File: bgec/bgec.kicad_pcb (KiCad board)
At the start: 2 copper layers, 10 parts

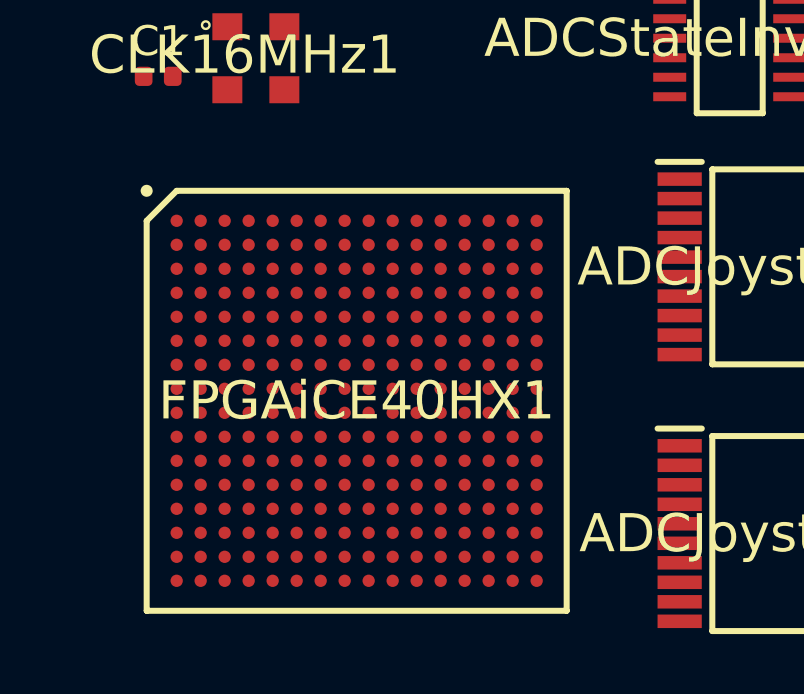
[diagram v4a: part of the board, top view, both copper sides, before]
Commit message: Switch to official footprint for the FPGA
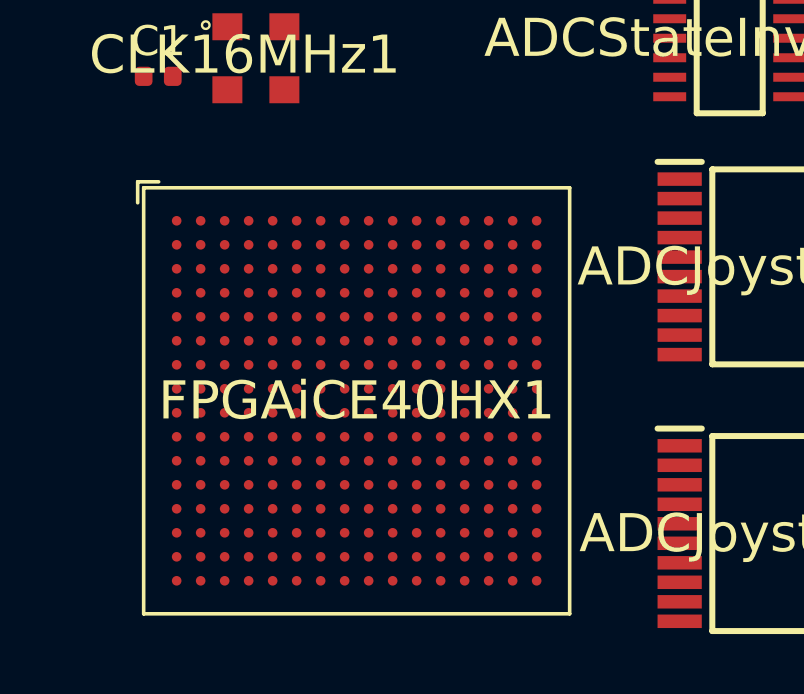
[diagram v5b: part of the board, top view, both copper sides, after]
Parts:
- FPGAiCE40HX1: footprint bgec:BGA256C80P16X16_1400X1400X170 -> bgec:BGA-256_14.0x14.0mm_Layout16x16_P0.8mm_Ball0.45mm_Pad0.32mm_NSMD

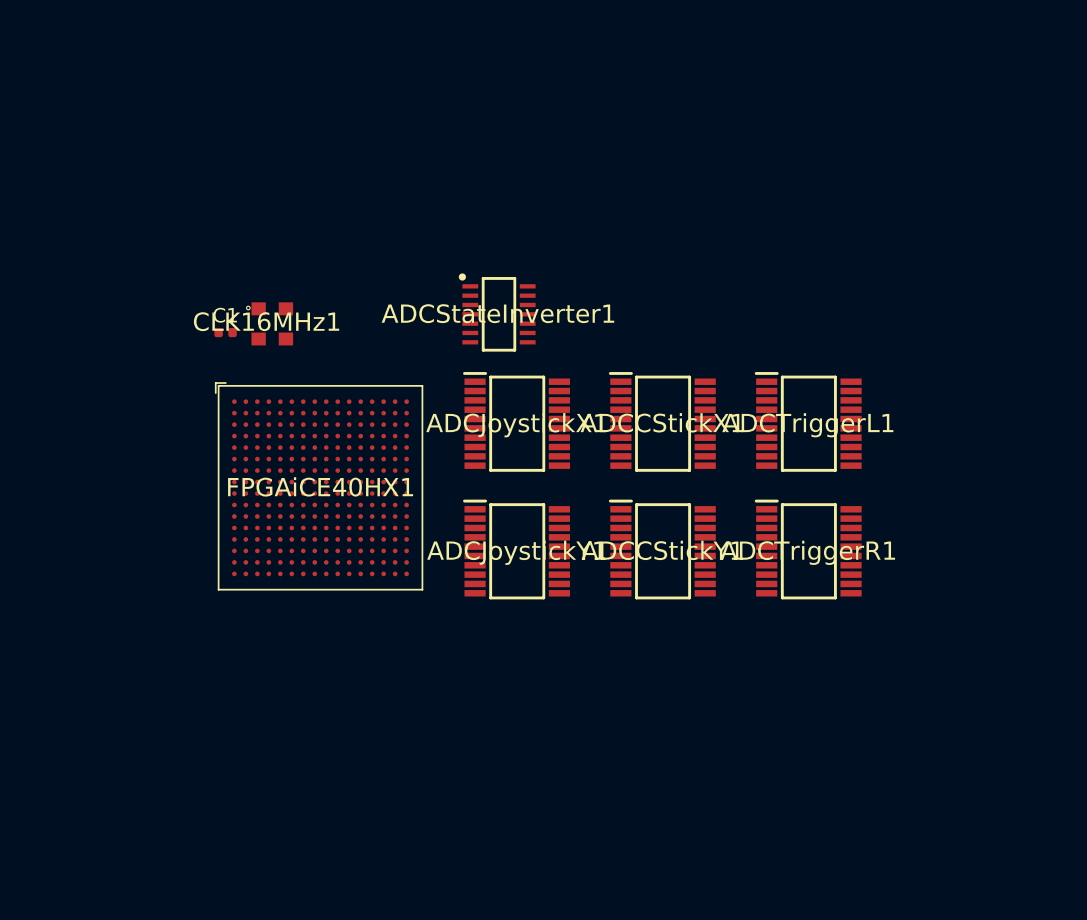
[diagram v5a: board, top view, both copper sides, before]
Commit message: Switch to better FPGA for routing
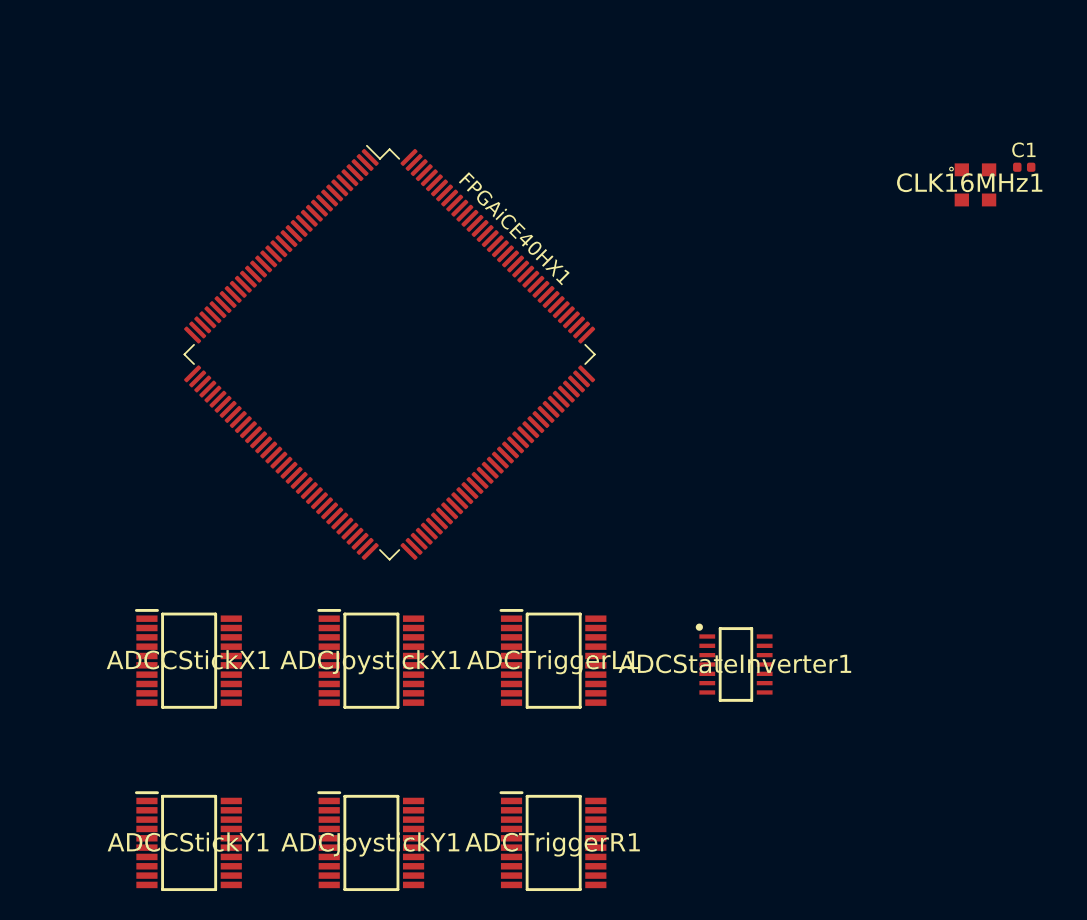
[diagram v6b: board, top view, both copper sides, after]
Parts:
- FPGAiCE40HX1: value ICE40HX8K-CT256 -> ICE40HX4K-TQ144; footprint bgec:BGA-256_14.0x14.0mm_Layout16x16_P0.8mm_Ball0.45mm_Pad0.32mm_NSMD -> Package_QFP:TQFP-144_20x20mm_P0.5mm
- moved C1 56.8 mm to (182.6, 97.7)
- moved CLK16MHz1 49.9 mm to (179.2, 98.9)
- moved ADCCStickY1 38.8 mm to (124.5, 144.8)
- moved ADCCStickX1 36.9 mm to (124.5, 132.1)
- moved ADCStateInverter1 29.5 mm to (162.6, 132.3)
- moved ADCTriggerR1 27.0 mm to (149.9, 144.8)
- moved ADCTriggerL1 24.3 mm to (149.9, 132.1)
- moved ADCJoystickY1 22.7 mm to (137.2, 144.8)
- moved ADCJoystickX1 19.4 mm to (137.2, 132.1)
- moved FPGAiCE40HX1 10.5 mm to (138.4, 110.7), turned to 315 degrees
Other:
- copper layers 2 -> 4

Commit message: Add more ADC connections
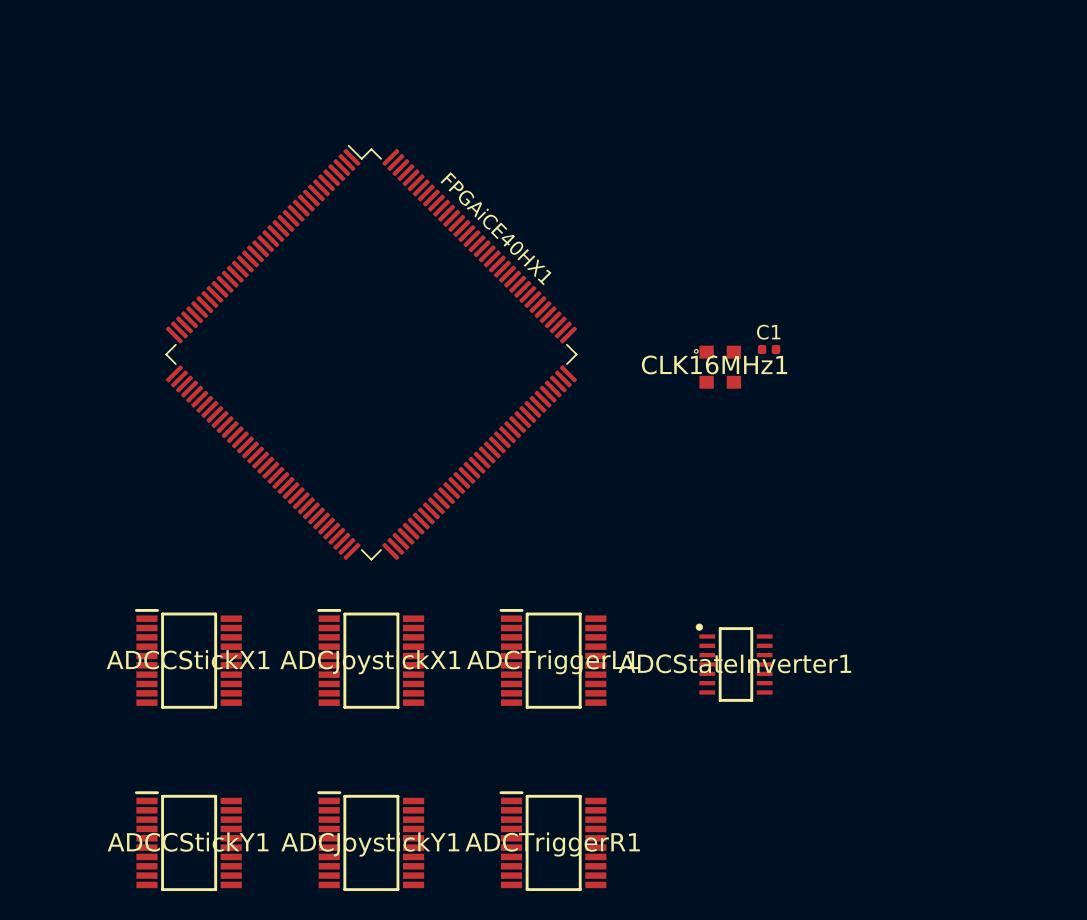
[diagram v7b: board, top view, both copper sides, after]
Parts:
- moved C1 21.8 mm to (164.9, 110.4)
- moved CLK16MHz1 21.8 mm to (161.5, 111.6)
- moved FPGAiCE40HX1 1.27 mm to (137.2, 110.7)
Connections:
- ADCCStickX1 pad 1: Net-(ADCCStickX1-Pad1) -> CStickXDB2
- ADCCStickX1 pad 16: Net-(ADCCStickX1-Pad16) -> CStickXDB7
- ADCCStickX1 pad 17: Net-(ADCCStickX1-Pad17) -> CStickXDB6
- ADCCStickX1 pad 18: Net-(ADCCStickX1-Pad18) -> CStickXDB5
- ADCCStickX1 pad 19: Net-(ADCCStickX1-Pad19) -> CStickXDB4
- ADCCStickX1 pad 2: Net-(ADCCStickX1-Pad2) -> CStickXDB1
- ADCCStickX1 pad 20: Net-(ADCCStickX1-Pad20) -> CStickXDB3
- ADCCStickX1 pad 3: Net-(ADCCStickX1-Pad3) -> CStickXDB0
- ADCCStickY1 pad 1: Net-(ADCCStickY1-Pad1) -> CStickYDB2
- ADCCStickY1 pad 16: Net-(ADCCStickY1-Pad16) -> CStickYDB7
- ADCCStickY1 pad 17: Net-(ADCCStickY1-Pad17) -> CStickYDB6
- ADCCStickY1 pad 18: Net-(ADCCStickY1-Pad18) -> CStickYDB5
- ADCCStickY1 pad 19: Net-(ADCCStickY1-Pad19) -> CStickYDB4
- ADCCStickY1 pad 2: Net-(ADCCStickY1-Pad2) -> CStickYDB1
- ADCCStickY1 pad 20: Net-(ADCCStickY1-Pad20) -> CStickYDB3
- ADCCStickY1 pad 3: Net-(ADCCStickY1-Pad3) -> CStickYDB0
- FPGAiCE40HX1 pad 10: Net-(FPGAiCE40HX1-Pad10) -> CStickXDB2
- FPGAiCE40HX1 pad 11: Net-(FPGAiCE40HX1-Pad11) -> CStickXDB1
- FPGAiCE40HX1 pad 12: Net-(FPGAiCE40HX1-Pad12) -> CStickXDB0
- FPGAiCE40HX1 pad 2: Net-(FPGAiCE40HX1-Pad2) -> CStickXEOC
- FPGAiCE40HX1 pad 23: Net-(FPGAiCE40HX1-Pad23) -> CStickYEOC
- FPGAiCE40HX1 pad 24: Net-(FPGAiCE40HX1-Pad24) -> CStickYDB7
- FPGAiCE40HX1 pad 25: Net-(FPGAiCE40HX1-Pad25) -> CStickYDB6
- FPGAiCE40HX1 pad 26: Net-(FPGAiCE40HX1-Pad26) -> CStickYDB5
- FPGAiCE40HX1 pad 28: Net-(FPGAiCE40HX1-Pad28) -> CStickYDB4
- FPGAiCE40HX1 pad 29: Net-(FPGAiCE40HX1-Pad29) -> CStickYDB3
- FPGAiCE40HX1 pad 3: Net-(FPGAiCE40HX1-Pad3) -> CStickXDB7
- FPGAiCE40HX1 pad 31: Net-(FPGAiCE40HX1-Pad31) -> CStickYDB2
- FPGAiCE40HX1 pad 32: Net-(FPGAiCE40HX1-Pad32) -> CStickYDB1
- FPGAiCE40HX1 pad 33: Net-(FPGAiCE40HX1-Pad33) -> CStickYDB0
- FPGAiCE40HX1 pad 4: Net-(FPGAiCE40HX1-Pad4) -> CStickXDB6
- FPGAiCE40HX1 pad 7: Net-(FPGAiCE40HX1-Pad7) -> CStickXDB5
- FPGAiCE40HX1 pad 8: Net-(FPGAiCE40HX1-Pad8) -> CStickXDB4
- FPGAiCE40HX1 pad 9: Net-(FPGAiCE40HX1-Pad9) -> CStickXDB3
